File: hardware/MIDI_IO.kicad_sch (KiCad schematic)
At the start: 12 parts, among them J1 MIDI In, J7 MIDI Through, Q1 MMBT5551L, Q2 MMBT5551L, U1 EL3H7(C)(TA)-G

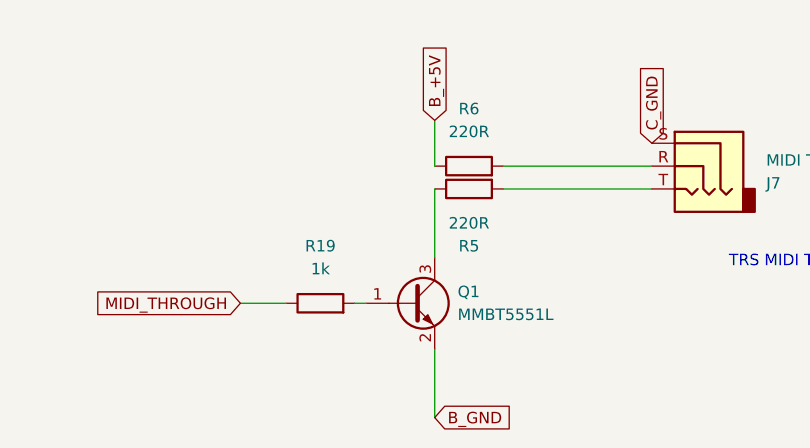
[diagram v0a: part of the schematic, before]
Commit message: main board rev 4: fix midi thru, led arrangement, glide cap value. fix sync trigger output
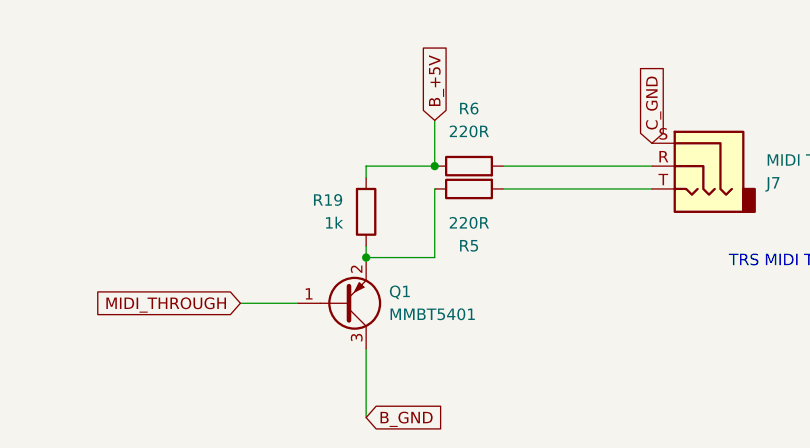
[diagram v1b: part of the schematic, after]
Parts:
- removed Q1: MMBT5551L, Package_TO_SOT_SMD:SOT-23, symbol Transistor_BJT:MMBT5551L
- added Q1: MMBT5401, Package_TO_SOT_SMD:SOT-23, symbol Transistor_BJT:Q_PNP_BEC
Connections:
- net B_+5V: now also R19.2
- net B_GND: now also Q1.3 (C)
- net MIDI_IN: now also Q1.1 (B); no longer R19.1
- net at R5.1: now also R19.1, Q1.2 (E)
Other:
- moved on the sheet: R19
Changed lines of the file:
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@@
 	(paper "A4")
 	(title_block
-		(rev "3")
+		(rev "4")
 	)
 	(text "TRS MIDI Type A"
@@
 	)
 	(junction
+		(at 77.47 116.84)
+		(diameter 0)
+		(color 0 0 0 0)
+	)
+	(junction
 		(at 86.36 53.34)
 		(diameter 0)
@@
 	)
 	(junction
+		(at 69.85 127)
+		(diameter 0)
+		(color 0 0 0 0)
+	)
+	(junction
 		(at 107.95 50.8)
 		(diameter 0)
@@
 	(wire
 		(pts
-			(xy 77.47 144.78) (xy 77.47 137.16)
+			(xy 69.85 137.16) (xy 69.85 144.78)
 		)
 		(stroke
@@
 	(wire
 		(pts
-			(xy 55.88 132.08) (xy 60.96 132.08)
+			(xy 55.88 132.08) (xy 62.23 132.08)
 		)
 		(stroke
@@
 	(wire
 		(pts
-			(xy 68.58 132.08) (xy 69.85 132.08)
+			(xy 69.85 118.11) (xy 69.85 116.84)
 		)
 		(stroke
@@
 	(wire
 		(pts
+			(xy 69.85 125.73) (xy 69.85 127)
+		)
+		(stroke
+			(width 0)
+			(type default)
+		)
+	)
+	(wire
+		(pts
 			(xy 85.09 119.38) (xy 101.6 119.38)
 		)
@@
 	(wire
 		(pts
+			(xy 69.85 116.84) (xy 77.47 116.84)
+		)
+		(stroke
+			(width 0)
+			(type default)
+		)
+	)
+	(wire
+		(pts
 			(xy 69.85 53.34) (xy 86.36 53.34)
 		)
@@
 		(pts
 			(xy 127 34.29) (xy 127 36.83)
+		)
+		(stroke
+			(width 0)
+			(type default)
+		)
+	)
+	(wire
+		(pts
+			(xy 69.85 127) (xy 77.47 127)
 		)
 		(stroke
@@
 	(global_label "B_GND"
 		(shape input)
-		(at 77.47 144.78 0)
+		(at 69.85 144.78 0)
 		(fields_autoplaced yes)
 		(effects
@@
 		)
 		(property "Intersheetrefs" "${INTERSHEET_REFS}"
-			(at 86.5633 144.78 0)
+			(at 78.9433 144.78 0)
 			(effects
 				(font
@@
 	)
 	(symbol
-		(lib_id "Transistor_BJT:MMBT5551L")
-		(at 74.93 132.08 0)
-		(unit 1)
-		(exclude_from_sim no)
-		(in_bom yes)
-		(on_board yes)
-		(dnp no)
-		(fields_autoplaced yes)
-		(property "Reference" "Q1"
-			(at 80.01 130.8099 0)
-			(effects
-				(font
-					(size 1.27 1.27)
-				)
-				(justify left)
-			)
-		)
-		(property "Value" "MMBT5551L"
-			(at 80.01 133.3499 0)
-			(effects
-				(font
-					(size 1.27 1.27)
-				)
-				(justify left)
-			)
-		)
-		(property "Footprint" "Package_TO_SOT_SMD:SOT-23"
-			(at 80.01 133.985 0)
-			(effects
-				(font
-					(size 1.27 1.27)
-					(italic yes)
-				)
-				(justify left)
-				(hide yes)
-			)
-		)
-		(property "Datasheet" "www.onsemi.com/pub/Collateral/MMBT5550LT1-D.PDF"
-			(at 74.93 132.08 0)
-			(effects
-				(font
-					(size 1.27 1.27)
-				)
-				(justify left)
-				(hide yes)
-			)
-		)
-		(property "Description" "0.6A Ic, 160V Vce, NPN Transistor, SOT-23"
-			(at 74.93 132.08 0)
-			(effects
-				(font
-					(size 1.27 1.27)
-				)
-				(hide yes)
-			)
-		)
-		(property "Sim.Device" "NPN"
-			(at 74.93 132.08 0)
-			(effects
-				(font
-					(size 1.27 1.27)
-				)
-				(hide yes)
-			)
-		)
-		(property "Sim.Pins" "1=B 2=E 3=C"
-			(at 74.93 132.08 0)
-			(effects
-				(font
-					(size 1.27 1.27)
-				)
-				(hide yes)
-			)
-		)
-		(property "LCSC" "C2145"
-			(at 74.93 132.08 0)
-			(effects
-				(font
-					(size 1.27 1.27)
-				)
-				(hide yes)
-			)
-		)
-		(pin "1"
-		)
-		(pin "3"
-		)
-		(pin "2"
-		)
-		(instances
-			(project ""
-				(path "/dc24635f-92c0-45e1-9dcb-753bde3bb041/957f6260-dd24-4429-8083-f8ea2da55485"
-					(reference "Q1")
-					(unit 1)
-				)
-			)
-		)
-	)
-	(symbol
 		(lib_id "Diode:1N4148WS")
 		(at 86.36 49.53 270)
@@
 				(path "/dc24635f-92c0-45e1-9dcb-753bde3bb041/957f6260-dd24-4429-8083-f8ea2da55485"
 					(reference "J1")
+					(unit 1)
+				)
+			)
+		)
+	)
+	(symbol
+		(lib_id "Transistor_BJT:Q_PNP_BEC")
+		(at 67.31 132.08 0)
+		(mirror x)
+		(unit 1)
+		(exclude_from_sim no)
+		(in_bom yes)
+		(on_board yes)
+		(dnp no)
+		(fields_autoplaced yes)
+		(property "Reference" "Q1"
+			(at 72.39 130.8099 0)
+			(effects
+				(font
+					(size 1.27 1.27)
+				)
+				(justify left)
+			)
+		)
+		(property "Value" "MMBT5401"
+			(at 72.39 133.3499 0)
+			(effects
+				(font
+					(size 1.27 1.27)
+				)
+				(justify left)
+			)
+		)
+		(property "Footprint" "Package_TO_SOT_SMD:SOT-23"
+			(at 72.39 134.62 0)
+			(effects
+				(font
+					(size 1.27 1.27)
+				)
+				(hide yes)
+			)
+		)
+		(property "Datasheet" "~"
+			(at 67.31 132.08 0)
+			(effects
+				(font
+					(size 1.27 1.27)
+				)
+				(hide yes)
+			)
+		)
+		(property "Description" "PNP transistor, base/emitter/collector"
+			(at 67.31 132.08 0)
+			(effects
+				(font
+					(size 1.27 1.27)
+				)
+				(hide yes)
+			)
+		)
+		(property "Sim.Device" "PNP"
+			(at 67.31 132.08 0)
+			(effects
+				(font
+					(size 1.27 1.27)
+				)
+				(hide yes)
+			)
+		)
+		(property "Sim.Pins" "1=B 2=E 3=C"
+			(at 67.31 132.08 0)
+			(effects
+				(font
+					(size 1.27 1.27)
+				)
+				(hide yes)
+			)
+		)
+		(property "LCSC" "C8326"
+			(at 67.31 132.08 0)
+			(effects
+				(font
+					(size 1.27 1.27)
+				)
+				(hide yes)
+			)
+		)
+		(pin "2"
+		)
+		(pin "3"
+		)
+		(pin "1"
+		)
+		(instances
+			(project ""
+				(path "/dc24635f-92c0-45e1-9dcb-753bde3bb041/957f6260-dd24-4429-8083-f8ea2da55485"
+					(reference "Q1")
 					(unit 1)
 				)
@@
 	(symbol
 		(lib_id "Device:R")
-		(at 64.77 132.08 90)
+		(at 69.85 121.92 0)
+		(mirror x)
 		(unit 1)
 		(exclude_from_sim no)
@@
 		(on_board yes)
 		(dnp no)
-		(fields_autoplaced yes)
 		(property "Reference" "R19"
-			(at 64.77 125.73 90)
-			(effects
-				(font
-					(size 1.27 1.27)
-				)
+			(at 67.31 120.6499 0)
+			(effects
+				(font
+					(size 1.27 1.27)
+				)
+				(justify right)
 			)
 		)
 		(property "Value" "1k"
-			(at 64.77 128.27 90)
-			(effects
-				(font
-					(size 1.27 1.27)
-				)
+			(at 67.31 123.1899 0)
+			(effects
+				(font
+					(size 1.27 1.27)
+				)
+				(justify right)
 			)
 		)
 		(property "Footprint" "Resistor_SMD:R_0603_1608Metric"
-			(at 64.77 133.858 90)
+			(at 68.072 121.92 90)
 			(effects
 				(font
@@
 		)
 		(property "Datasheet" "~"
-			(at 64.77 132.08 0)
+			(at 69.85 121.92 0)
 			(effects
 				(font
@@
 		)
 		(property "Description" "Resistor"
-			(at 64.77 132.08 0)
+			(at 69.85 121.92 0)
 			(effects
 				(font
@@
 		)
 		(property "LCSC" "C21190"
-			(at 64.77 132.08 90)
+			(at 69.85 121.92 90)
 			(effects
 				(font
@@
 		)
 		(property "JLCPCB_IGNORE" ""
-			(at 64.77 132.08 90)
-			(effects
-				(font
+			(at 69.85 121.92 90)
+			(effects
+				(font
